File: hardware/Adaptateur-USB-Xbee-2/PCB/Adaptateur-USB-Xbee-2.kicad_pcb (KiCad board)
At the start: 2 copper layers, 57.5 x 56.6 mm, 30 parts, among them J1 Conn_Coaxial, J2 USB_C_Receptacle_USB2.0, SW1 SW_Push, SW2 SW_SPDT, U1 FT231XS, U2 NCP1117-3.3_SOT223, U3A1 XBee_RR_MMT, U3B1 XBEE-3-TH, U4 74AHC1G08

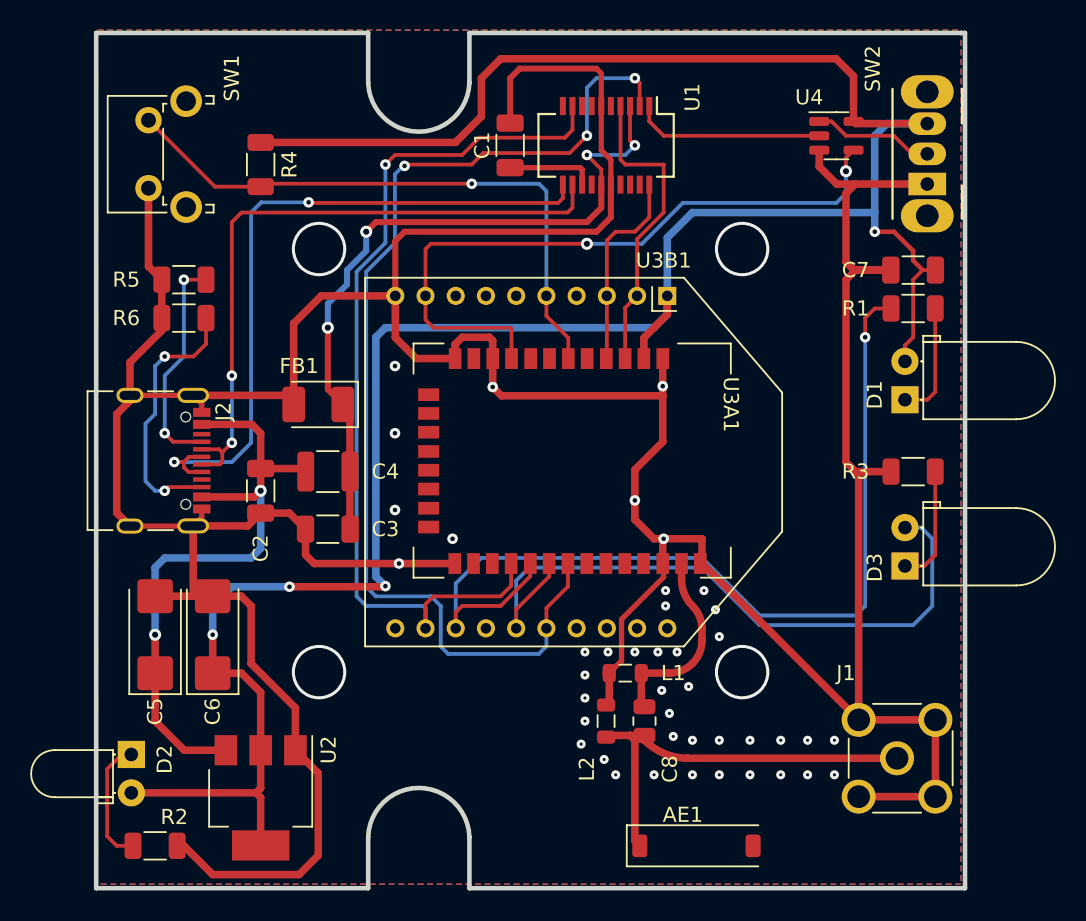
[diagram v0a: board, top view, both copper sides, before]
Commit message: Corrections mineurs sur le PCB, V1.1
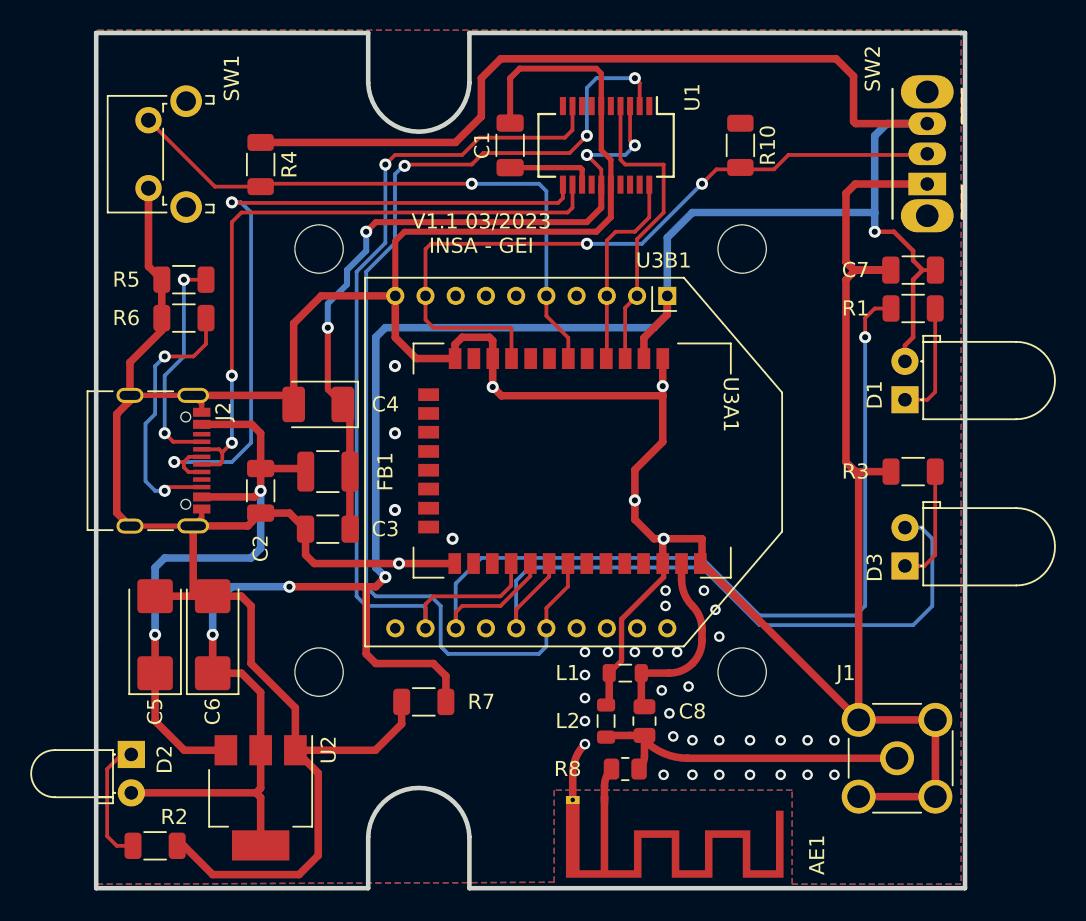
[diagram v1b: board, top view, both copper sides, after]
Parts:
- removed U4: 74AHC1G08, Package_TO_SOT_SMD:SOT-23-5
- added H1: MountingHole, MountingHole:MountingHole_3.2mm_M3, F.Cu at (99.8, 98.3)
- added H2: MountingHole, MountingHole:MountingHole_3.2mm_M3, F.Cu at (127.8, 98.3)
- added H3: MountingHole, MountingHole:MountingHole_3.2mm_M3, F.Cu at (127.8, 126.3)
- added H4: MountingHole, MountingHole:MountingHole_3.2mm_M3, F.Cu at (99.8, 126.3)
- added R10: 0R, Resistor_SMD:R_1206_3216Metric, F.Cu at (127.6, 91.4)
- added R7: 100R, Resistor_SMD:R_1206_3216Metric, F.Cu at (106.7, 128.3)
- added R8: 0 R, Resistor_SMD:R_0805_2012Metric, F.Cu at (120.0, 132.7)
- AE1: value 2600AT44A0600E -> Antenna_Chip; footprint INSA:Johanson_2600AT44A0600E -> RF_Antenna:Texas_SWRA117D_2.4GHz_Left
- moved AE1 6.01 mm to (118.6, 134.8), turned to 180 degrees
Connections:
- AE1 pad 2: unconnected-(AE1-Pad2) -> GND
- C8 pad 2: Net-(AE1-Pad1) -> /RF
- J1 pad 1: Net-(AE1-Pad1) -> /RF
- L2 pad 2: Net-(AE1-Pad1) -> /RF
- SW2 pad 2: Net-(SW2-Pad2) -> /SLEEP_RQ
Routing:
- net Net-(AE1-Pad1): track 27.5 -> 2.16 mm
- net /RF: track 0.00 -> 22.2 mm
- net /USART_DTR: track 12.7 -> 0.00 mm
- net +3.3V: track 173.3 -> 184.9 mm
- net GND: track 292.1 -> 301.1 mm, vias 42 -> 40
- net Net-(SW2-Pad2): track 7.14 -> 0.00 mm
- net /USB_DP: track 46.4 -> 49.0 mm
- net /SLEEP_RQ: track 45.0 -> 47.4 mm
- net (no net): vias 4 -> 0
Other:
- board text added: "V1.1 03/2023 INSA - GEI"

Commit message: Commit avant nouveau projet
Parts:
- C5: footprint Capacitor_Tantalum_SMD:CP_EIA-6032-28_Kemet-C_Pad2.25x2.35mm_HandSolder -> Capacitor_SMD:C_1206_3216Metric
- C6: value 10µF -> 22µF; footprint Capacitor_Tantalum_SMD:CP_EIA-6032-28_Kemet-C_Pad2.25x2.35mm_HandSolder -> Capacitor_SMD:C_1206_3216Metric
- U2: value NCP1117-3.3_SOT223 -> AZ1117IH-3.3_SOT223
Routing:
- net +3.3V: track 184.9 -> 183.8 mm
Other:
- board text added: "V1.1b 03/2023 INSA - GEI"
- board text removed: "V1.1 03/2023 INSA - GEI"
